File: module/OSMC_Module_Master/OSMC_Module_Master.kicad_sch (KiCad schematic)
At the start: 10 parts, among them SW1 SW_Push, SW2 SW_Push, SW3 SW_Push, U1 OSMC Module Board w/pins, U2 24LC02BT-I/OT, U3 PCF8574DWR

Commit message: reviewed PCBs
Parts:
- added JP1, JP2, JP3: SolderJumper_2_Bridged, Jumper:SolderJumper-2_P1.3mm_Bridged2Bar_Pad1.0x1.5mm, symbol Jumper:SolderJumper_2_Bridged
- D1, D2, D3, D4: footprint LED_THT:LED_D5.0mm -> LED_SMD:LED_0603_1608Metric_Pad1.05x0.95mm_HandSolder
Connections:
- net 3v3: now also D1.1 (K), D2.1 (K), D3.1 (K), D4.1 (K), U3.16 (VCC)
- net 5V: no longer U3.16 (VCC)
- net GND: now also JP1.2 (B), JP2.2 (B), JP3.2 (B); no longer D1.1 (K), D2.1 (K), D3.1 (K), D4.1 (K), U3.1 (A0), U3.2 (A1), U3.3 (A2)
- net A2: now reaches U1.18 (A3)
- net A2: now also U3.3 (A2), JP3.1 (A)
- net A1: now reaches U1.19 (A2)
- net A1: now also U3.2 (A1), JP2.1 (A)
- net A0: now reaches U1.20 (A1)
- net A0: now also U3.1 (A0), JP1.1 (A)
- no-connect marks 0 -> 2
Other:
- moved on the sheet: D1, D2, D3, D4

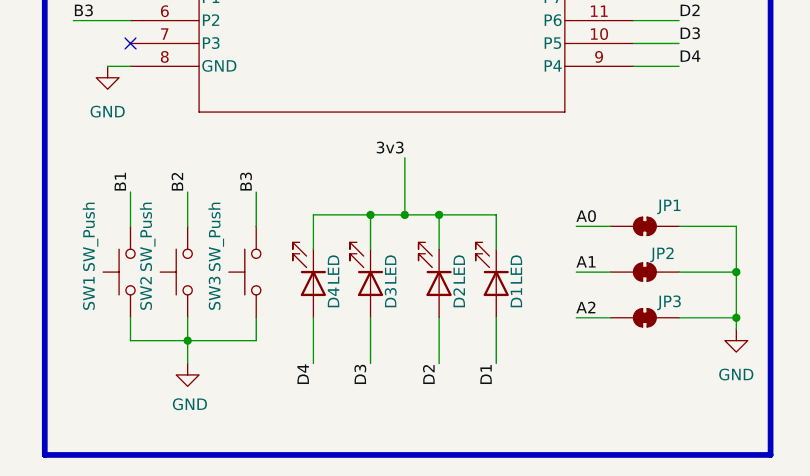
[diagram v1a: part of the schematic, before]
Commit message: fixed diode direction
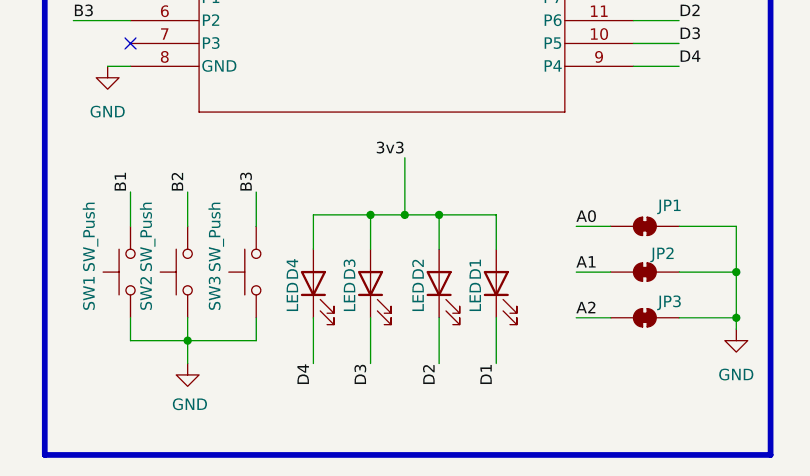
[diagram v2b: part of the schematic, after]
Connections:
- net 3v3: now also D1.2 (A), D2.2 (A), D3.2 (A), D4.2 (A); no longer D1.1 (K), D2.1 (K), D3.1 (K), D4.1 (K)
- net D1: now also D1.1 (K); no longer D1.2 (A)
- net D2: now also D2.1 (K); no longer D2.2 (A)
- net D3: now also D3.1 (K); no longer D3.2 (A)
- net D4: now also D4.1 (K); no longer D4.2 (A)
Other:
- moved on the sheet: D1, D2, D3, D4
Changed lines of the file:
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@@
 	(symbol
 		(lib_id "Library:LED")
-		(at 97.79 165.1 270)
+		(at 97.79 165.1 90)
 		(unit 1)
 		(exclude_from_sim no)
@@
 		(dnp no)
 		(property "Reference" "D3"
-			(at 100.076 166.6875 0)
+			(at 95.504 163.5125 0)
 			(effects
 				(font
@@
 		)
 		(property "Value" "LED"
-			(at 100.076 163.576 0)
+			(at 95.504 166.624 0)
 			(effects
 				(font
@@
 	(symbol
 		(lib_id "Library:LED")
-		(at 105.41 165.1 270)
+		(at 105.41 165.1 90)
 		(unit 1)
 		(exclude_from_sim no)
@@
 		(dnp no)
 		(property "Reference" "D2"
-			(at 107.696 166.6875 0)
+			(at 103.124 163.5125 0)
 			(effects
 				(font
@@
 		)
 		(property "Value" "LED"
-			(at 107.696 163.576 0)
+			(at 103.124 166.624 0)
 			(effects
 				(font
@@
 	(symbol
 		(lib_id "Library:LED")
-		(at 91.44 165.1 270)
+		(at 91.44 165.1 90)
 		(unit 1)
 		(exclude_from_sim no)
@@
 		(dnp no)
 		(property "Reference" "D4"
-			(at 93.726 166.6875 0)
+			(at 89.154 163.5125 0)
 			(effects
 				(font
@@
 		)
 		(property "Value" "LED"
-			(at 93.726 163.576 0)
+			(at 89.154 166.624 0)
 			(effects
 				(font
@@
 	(symbol
 		(lib_id "Library:LED")
-		(at 111.76 165.1 270)
+		(at 111.76 165.1 90)
 		(unit 1)
 		(exclude_from_sim no)
@@
 		(dnp no)
 		(property "Reference" "D1"
-			(at 114.046 166.6875 0)
+			(at 109.474 163.5125 0)
 			(effects
 				(font
@@
 		)
 		(property "Value" "LED"
-			(at 114.046 163.576 0)
-			(effects
-				(font
+			(at 109.474 166.624 0)
+			(effects
+				(font
